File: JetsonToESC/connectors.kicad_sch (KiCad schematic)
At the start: 13 parts, among them J1 Conn_01x12, J2 Conn_01x02, J3 Conn_01x02, J4 Screw_Terminal_01x01, J5 Screw_Terminal_01x01

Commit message: Edit mounting holes to 3mm
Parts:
- H1, H2, H3, H4: footprint TestPoint:TestPoint_Plated_Hole_D2.0mm -> TestPoint:TestPoint_Plated_Hole_D3.0mm
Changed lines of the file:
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@@
 			)
 		)
-		(property "Footprint" "TestPoint:TestPoint_Plated_Hole_D2.0mm"
+		(property "Footprint" "TestPoint:TestPoint_Plated_Hole_D3.0mm"
 			(at 90.17 21.59 0)
 			(effects
@@
 			)
 		)
-		(property "Footprint" "TestPoint:TestPoint_Plated_Hole_D2.0mm"
+		(property "Footprint" "TestPoint:TestPoint_Plated_Hole_D3.0mm"
 			(at 111.76 31.75 0)
 			(effects
@@
 			)
 		)
-		(property "Footprint" "TestPoint:TestPoint_Plated_Hole_D2.0mm"
+		(property "Footprint" "TestPoint:TestPoint_Plated_Hole_D3.0mm"
 			(at 90.17 31.75 0)
 			(effects
@@
 			)
 		)
-		(property "Footprint" "TestPoint:TestPoint_Plated_Hole_D2.0mm"
+		(property "Footprint" "TestPoint:TestPoint_Plated_Hole_D3.0mm"
 			(at 111.76 21.59 0)
 			(effects

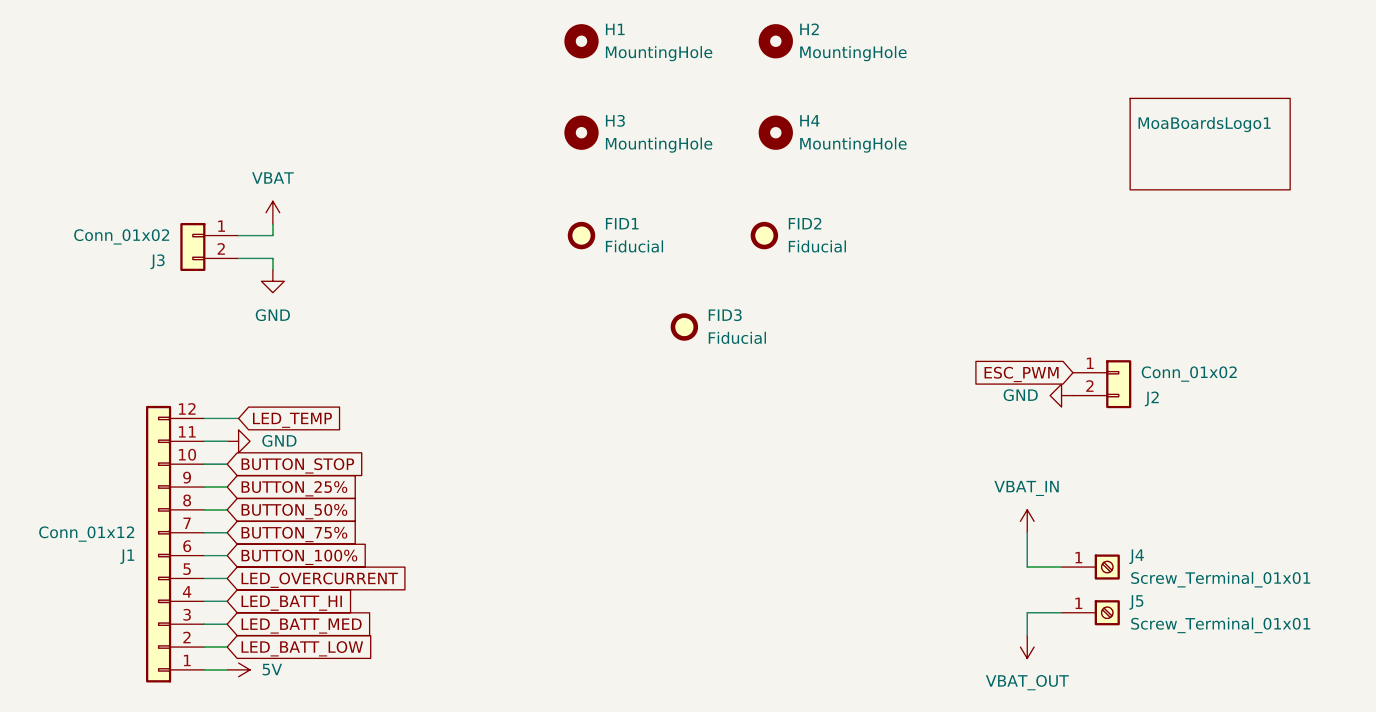
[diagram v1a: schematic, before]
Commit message: Changed connectors into moles microfit
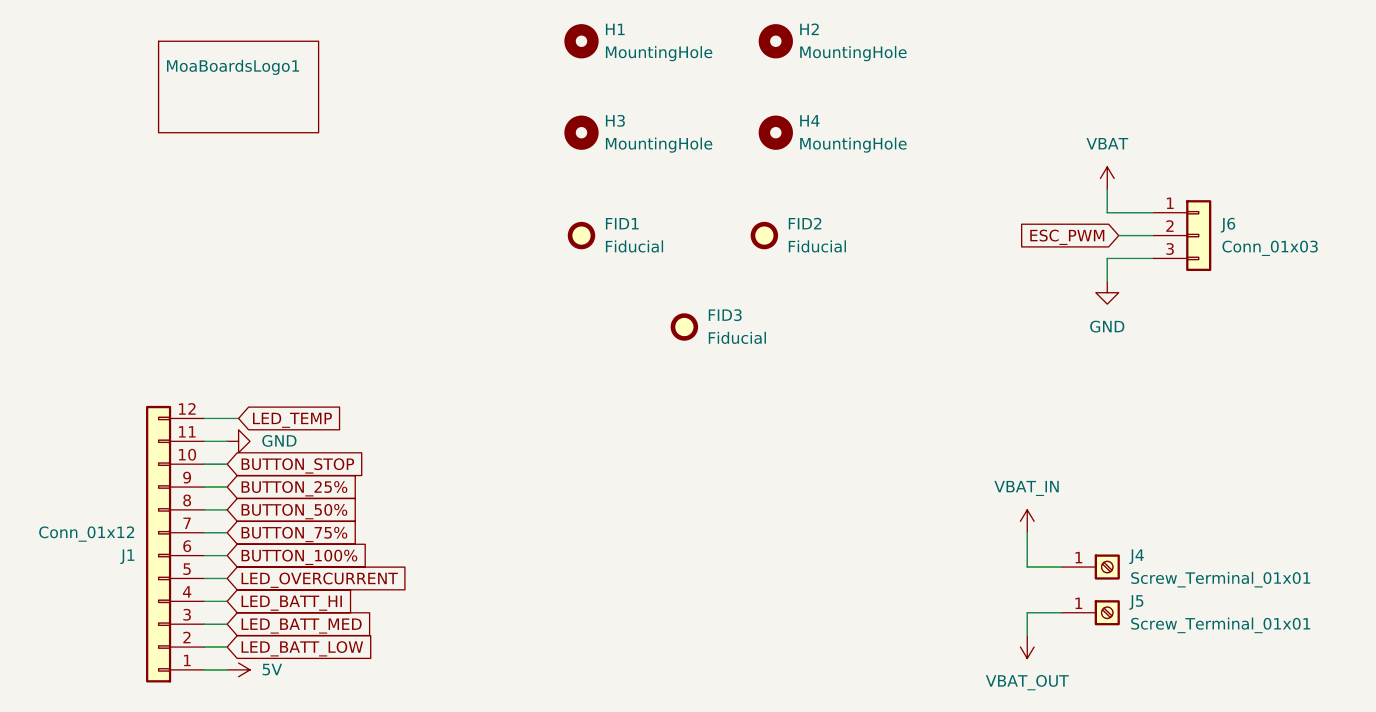
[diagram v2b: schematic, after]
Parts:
- removed J2, J3: Conn_01x02, Connector_PinHeader_2.54mm:PinHeader_1x02_P2.54mm_Horizontal, symbol Connector_Generic:Conn_01x02
- added J6: Conn_01x03, Connector_Molex:Molex_Micro-Fit_3.0_43650-0300_1x03_P3.00mm_Horizontal, symbol Connector_Generic:Conn_01x03
- J1: footprint Connector_PinHeader_2.54mm:PinHeader_1x12_P2.54mm_Horizontal -> Connector_Molex:Molex_Micro-Fit_3.0_43650-1200_1x12_P3.00mm_Horizontal
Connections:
- net ESC_PWM: now also J6.2 (Pin_2)
- net GND: now also J6.3 (Pin_3)
- net VBAT: now also J6.1 (Pin_1)
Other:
- moved on the sheet: MoaBoardsLogo1

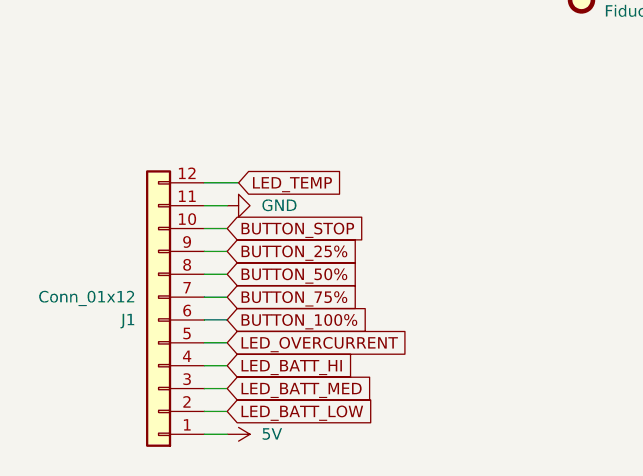
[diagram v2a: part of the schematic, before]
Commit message: Updated connector and temp sensor into IDC and NTC
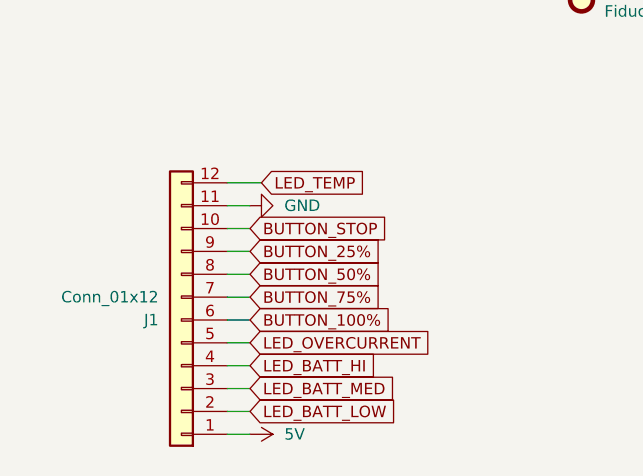
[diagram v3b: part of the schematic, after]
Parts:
- J1: footprint Connector_Molex:Molex_Micro-Fit_3.0_43650-1200_1x12_P3.00mm_Horizontal -> Connector_IDC:IDC-Header_2x06_P2.54mm_Vertical
- J6: footprint Connector_Molex:Molex_Micro-Fit_3.0_43650-0300_1x03_P3.00mm_Horizontal -> Connector_JST:JST_XH_B3B-XH-A_1x03_P2.50mm_Vertical
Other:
- moved on the sheet: J1
